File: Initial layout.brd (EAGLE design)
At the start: 152.4 x 127 mm, 50 parts, among them U2 TPS54540DDARQ1

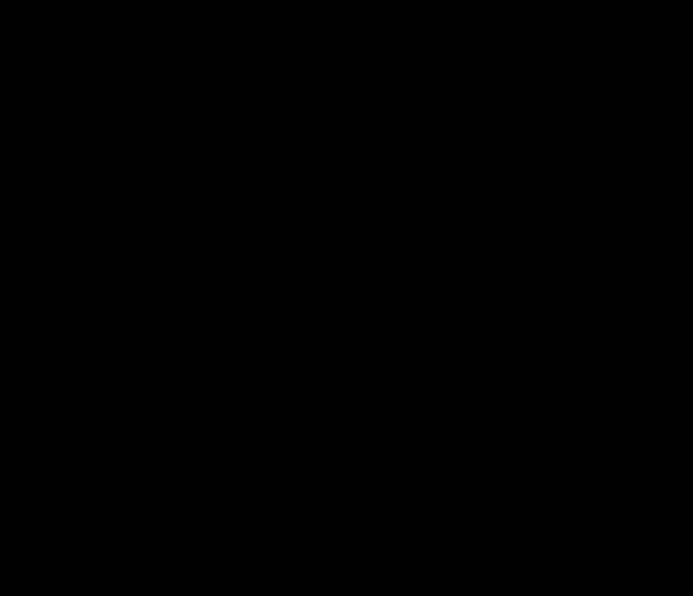
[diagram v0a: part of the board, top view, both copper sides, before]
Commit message: Added 4 pin clickmate for rj45
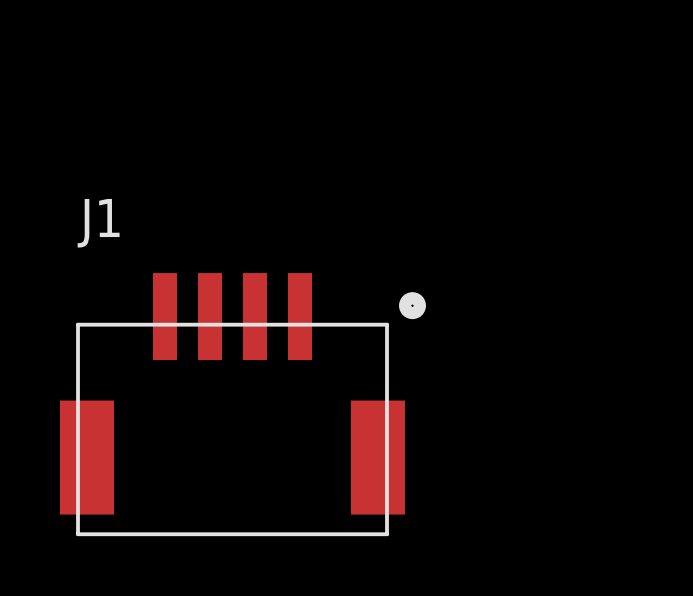
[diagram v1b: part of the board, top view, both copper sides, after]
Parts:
- added J1: 502585-0470, FormE:MOLEX-CLIKMATE-4-R/A
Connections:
- new net N$34: J1.1, U$2.38/A19
- new net N$35: J1.2, U$2.39/A20
- net GND: now also J1.3, J1.4
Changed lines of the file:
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@@
 <?xml version="1.0" encoding="utf-8"?>
 <!DOCTYPE eagle SYSTEM "eagle.dtd">
-<eagle version="8.5.0">
+<eagle version="8.6.0">
 <drawing>
 <settings>
@@
 <layers>
 <layer number="1" name="Top" color="4" fill="1" visible="yes" active="yes"/>
+<layer number="2" name="GND" color="11" fill="1" visible="yes" active="yes"/>
+<layer number="3" name="Route3" color="4" fill="3" visible="no" active="no"/>
+<layer number="4" name="Route4" color="1" fill="4" visible="no" active="no"/>
+<layer number="5" name="Route5" color="4" fill="4" visible="no" active="no"/>
+<layer number="6" name="Route6" color="1" fill="8" visible="no" active="no"/>
+<layer number="7" name="Route7" color="4" fill="8" visible="no" active="no"/>
+<layer number="8" name="Route8" color="1" fill="2" visible="no" active="no"/>
+<layer number="9" name="Route9" color="4" fill="2" visible="no" active="no"/>
+<layer number="10" name="Route10" color="1" fill="7" visible="no" active="no"/>
+<layer number="11" name="Route11" color="4" fill="7" visible="no" active="no"/>
+<layer number="12" name="Route12" color="1" fill="5" visible="no" active="no"/>
+<layer number="13" name="Route13" color="4" fill="5" visible="no" active="no"/>
+<layer number="14" name="Route14" color="1" fill="6" visible="no" active="no"/>
+<layer number="15" name="SUPPLY" color="13" fill="1" visible="yes" active="yes"/>
 <layer number="16" name="Bottom" color="1" fill="1" visible="yes" active="yes"/>
 <layer number="17" name="Pads" color="2" fill="1" visible="yes" active="yes"/>
@@
 </element>
 <element name="U3" library="FormE" package="SOIC8-N_MC" value="" x="8.25" y="87.41"/>
+<element name="J1" library="FormE" package="MOLEX-CLIKMATE-4-R/A" value="502585-0470" x="-7" y="26"/>
 </elements>
 <signals>
@@
 <wire x1="5.65" y1="88.045" x2="2.825" y2="88.045" width="0.254" layer="1"/>
 <wire x1="2.825" y1="88.045" x2="2.62" y2="88.25" width="0.254" layer="1"/>
+<contactref element="J1" pad="3"/>
+<contactref element="J1" pad="4"/>
 <wire x1="218" y1="39.43" x2="214.04" y2="39.78" width="0" layer="19" extent="1-1"/>
 <wire x1="206.98" y1="39.41" x2="214.04" y2="39.78" width="0" layer="19" extent="1-1"/>
@@
 <wire x1="5.65" y1="88.045" x2="10.85" y2="89.315" width="0" layer="19" extent="1-1"/>
 <wire x1="14.38" y1="81.83" x2="10.85" y2="89.315" width="0" layer="19" extent="1-1"/>
+<wire x1="-7.75" y1="29.7" x2="14.38" y2="81.83" width="0" layer="19" extent="1-1"/>
+<wire x1="-9.25" y1="29.7" x2="-7.75" y2="29.7" width="0" layer="19" extent="1-1"/>
 </signal>
 <signal name="+15V">
@@
 <wire x1="220.22" y1="59.35" x2="80.46" y2="123.33" width="0" layer="19" extent="1-1"/>
 </signal>
+<signal name="N$34">
+<contactref element="J1" pad="1"/>
+<contactref element="U$2" pad="38/A19"/>
+<wire x1="-4.75" y1="29.7" x2="85.54" y2="123.33" width="0" layer="19" extent="1-1"/>
+</signal>
+<signal name="N$35">
+<contactref element="J1" pad="2"/>
+<contactref element="U$2" pad="39/A20"/>
+<wire x1="-6.25" y1="29.7" x2="88.08" y2="123.33" width="0" layer="19" extent="1-1"/>
+</signal>
 </signals>

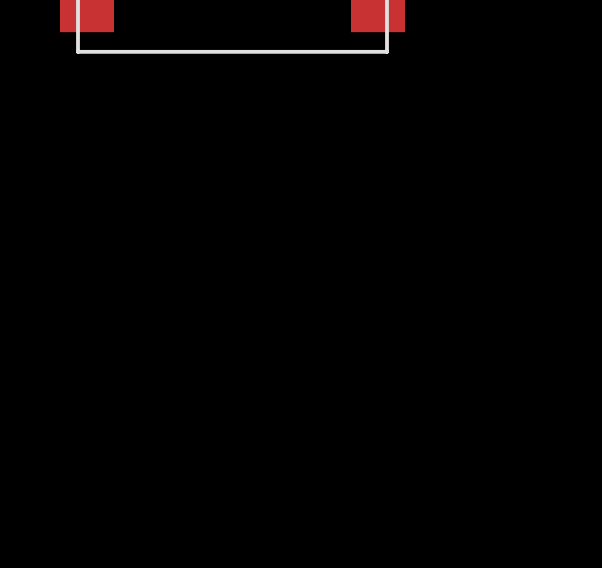
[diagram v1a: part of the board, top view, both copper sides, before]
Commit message: Added resistors for LEDs
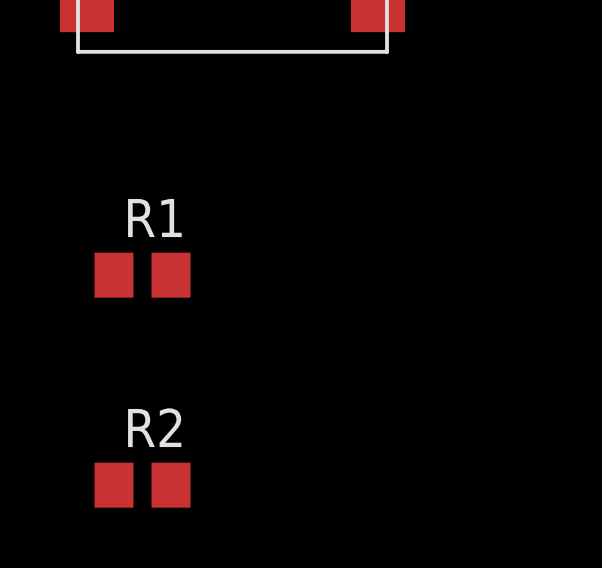
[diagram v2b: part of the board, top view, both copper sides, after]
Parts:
- added R1, R2: 100, rcl:R0805
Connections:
- new net N$41: R1.1, U$2.39/A20
- new net N$42: R2.1, U$2.38/A19
- net N$34: now also R2.2; no longer U$2.38/A19
- net N$35: now also R1.2; no longer U$2.39/A20
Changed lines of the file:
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@@
 <element name="U3" library="FormE" package="SOIC8-N_MC" value="" x="8.25" y="87.41"/>
 <element name="J1" library="FormE" package="MOLEX-CLIKMATE-4-R/A" value="502585-0470" x="-7" y="26"/>
+<element name="R1" library="rcl" package="R0805" value="100" x="-10" y="15"/>
+<element name="R2" library="rcl" package="R0805" value="100" x="-10" y="8"/>
 </elements>
 <signals>
@@
 <signal name="N$34">
 <contactref element="J1" pad="1"/>
-<contactref element="U$2" pad="38/A19"/>
-<wire x1="-4.75" y1="29.7" x2="85.54" y2="123.33" width="0" layer="19" extent="1-1"/>
+<contactref element="R2" pad="2"/>
+<wire x1="-9.05" y1="8" x2="-4.75" y2="29.7" width="0" layer="19" extent="1-1"/>
 </signal>
 <signal name="N$35">
 <contactref element="J1" pad="2"/>
+<contactref element="R1" pad="2"/>
+<wire x1="-9.05" y1="15" x2="-6.25" y2="29.7" width="0" layer="19" extent="1-1"/>
+</signal>
+<signal name="N$41">
 <contactref element="U$2" pad="39/A20"/>
-<wire x1="-6.25" y1="29.7" x2="88.08" y2="123.33" width="0" layer="19" extent="1-1"/>
+<contactref element="R1" pad="1"/>
+<wire x1="-10.95" y1="15" x2="88.08" y2="123.33" width="0" layer="19" extent="1-1"/>
+</signal>
+<signal name="N$42">
+<contactref element="U$2" pad="38/A19"/>
+<contactref element="R2" pad="1"/>
+<wire x1="-10.95" y1="8" x2="85.54" y2="123.33" width="0" layer="19" extent="1-1"/>
 </signal>
 </signals>

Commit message: Created Right Ear Board and made adjustments to Dash
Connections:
- removed net LBL: U$1.P$5, U$2.31/A12
- removed net RTDL: U$1.P$4, U$2.30
- new net NEO_PIXEL_PWM: U$1.P$4, U$2.21/A7
- new net SPARE_5: U$1.P$6
- net GND: now also U$1.P$5; no longer U$1.P$6
- net SERVO_PWM: now also U$2.22/A8; no longer U$2.29
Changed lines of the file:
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@@
 <contactref element="U$1" pad="P$19"/>
 <contactref element="U$1" pad="P$16"/>
-<contactref element="U$1" pad="P$6"/>
 <wire x1="5.65" y1="88.045" x2="2.825" y2="88.045" width="0.254" layer="1"/>
 <wire x1="2.825" y1="88.045" x2="2.62" y2="88.25" width="0.254" layer="1"/>
 <contactref element="J1" pad="3"/>
 <contactref element="J1" pad="4"/>
+<contactref element="U$1" pad="P$5"/>
 <wire x1="218" y1="39.43" x2="214.04" y2="39.78" width="0" layer="19" extent="1-1"/>
 <wire x1="206.98" y1="39.41" x2="214.04" y2="39.78" width="0" layer="19" extent="1-1"/>
@@
 <wire x1="236.05" y1="25.775" x2="227.34" y2="31.11" width="0" layer="19" extent="1-1"/>
 <wire x1="239.05" y1="26.41" x2="236.05" y2="25.775" width="0" layer="19" extent="1-1"/>
-<wire x1="224.22" y1="59.35" x2="218" y2="39.43" width="0" layer="19" extent="1-1"/>
-<wire x1="232.22" y1="67.35" x2="224.22" y2="59.35" width="0" layer="19" extent="1-1"/>
+<wire x1="228.22" y1="59.35" x2="218" y2="39.43" width="0" layer="19" extent="1-1"/>
+<wire x1="232.22" y1="67.35" x2="228.22" y2="59.35" width="0" layer="19" extent="1-1"/>
 <wire x1="244.22" y1="67.35" x2="232.22" y2="67.35" width="0" layer="19" extent="1-1"/>
 <wire x1="134.43" y1="36.84" x2="204.665" y2="31.22" width="0" layer="19" extent="1-1"/>
@@
 </signal>
 <signal name="SERVO_PWM">
-<contactref element="U$2" pad="29"/>
 <contactref element="U$1" pad="P$3"/>
-<wire x1="236.22" y1="59.35" x2="80.46" y2="108.09" width="0" layer="19" extent="1-1"/>
-</signal>
-<signal name="RTDL">
-<contactref element="U$1" pad="P$4"/>
-<contactref element="U$2" pad="30"/>
-<wire x1="232.22" y1="59.35" x2="77.92" y2="108.09" width="0" layer="19" extent="1-1"/>
-</signal>
-<signal name="LBL">
-<contactref element="U$1" pad="P$5"/>
-<contactref element="U$2" pad="31/A12"/>
-<wire x1="228.22" y1="59.35" x2="75.38" y2="108.09" width="0" layer="19" extent="1-1"/>
+<contactref element="U$2" pad="22/A8"/>
+<wire x1="236.22" y1="59.35" x2="121.1" y2="123.33" width="0" layer="19" extent="1-1"/>
 </signal>
 <signal name="N$27">
@@
 <wire x1="-10.95" y1="8" x2="85.54" y2="123.33" width="0" layer="19" extent="1-1"/>
 </signal>
+<signal name="NEO_PIXEL_PWM">
+<contactref element="U$1" pad="P$4"/>
+<contactref element="U$2" pad="21/A7"/>
+<wire x1="232.22" y1="59.35" x2="118.56" y2="123.33" width="0" layer="19" extent="1-1"/>
+</signal>
+<signal name="SPARE_5">
+<contactref element="U$1" pad="P$6"/>
+</signal>
 </signals>

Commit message: Defined Pins, Updated names on schematic
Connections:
- net N$13 renamed DOWN
- net N$15 renamed LEFT
- net N$17 renamed RIGHT
- net N$18 renamed DRS_FLAP
- net N$19 renamed UP
- net N$26 renamed CAN_RX
- net N$27 renamed DI1
- net N$28 renamed CAN_TX
- net N$3 renamed PADDLE
- net N$41 renamed RJ45_L1
- net N$42 renamed RJ45_L2
- removed net D2: JP2.6
- removed net N$16: U$2.3V3
- removed net NEO_PIXEL_PWM: U$1.P$4, U$2.21/A7
- new net DI2: JP2.6, U$1.P$4, U$2.21/A7
- net +3V3: now also U$2.3V3
- net SPARE_5: now also U$2.37/A18
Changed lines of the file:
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@@
 <contactref element="JP2" pad="5"/>
 </signal>
-<signal name="D2">
+<signal name="DI2">
 <contactref element="JP2" pad="6"/>
+<contactref element="U$1" pad="P$4"/>
+<contactref element="U$2" pad="21/A7"/>
+<wire x1="134.43" y1="72.4" x2="118.56" y2="123.33" width="0" layer="19" extent="1-1"/>
+<wire x1="232.22" y1="59.35" x2="134.43" y2="72.4" width="0" layer="19" extent="1-1"/>
 </signal>
 <signal name="D1">
@@
 <wire x1="10.85" y1="85.505" x2="12.625" y2="83.73" width="0.254" layer="1"/>
 <wire x1="12.625" y1="83.73" x2="14.38" y2="83.73" width="0.254" layer="1"/>
-</signal>
-<signal name="N$13">
+<contactref element="U$2" pad="3V3"/>
+<wire x1="14.38" y1="83.73" x2="95.7" y2="108.09" width="0" layer="19" extent="1-1"/>
+</signal>
+<signal name="DOWN">
 <contactref element="U$2" pad="25"/>
 </signal>
-<signal name="N$15">
+<signal name="LEFT">
 <contactref element="U$2" pad="26"/>
 </signal>
-<signal name="N$17">
+<signal name="RIGHT">
 <contactref element="U$2" pad="27"/>
 </signal>
-<signal name="N$18">
+<signal name="DRS_FLAP">
 <contactref element="U$2" pad="28"/>
 </signal>
@@
 <wire x1="242.22" y1="63.35" x2="14.38" y2="86.67" width="0" layer="19" extent="1-1"/>
 </signal>
-<signal name="N$3">
+<signal name="PADDLE">
 <contactref element="H1" pad="7"/>
 <contactref element="U$2" pad="32/A13"/>
 <wire x1="72.84" y1="108.09" x2="102.09" y2="101.474" width="0" layer="19" extent="1-1"/>
 </signal>
-<signal name="N$16">
-<contactref element="U$2" pad="3V3"/>
-</signal>
-<signal name="N$19">
+<signal name="UP">
 <contactref element="U$2" pad="24"/>
 </signal>
@@
 <wire x1="238.22" y1="63.35" x2="14.38" y2="88.57" width="0" layer="19" extent="1-1"/>
 </signal>
-<signal name="N$28">
+<signal name="CAN_TX">
 <contactref element="U3" pad="1"/>
 <contactref element="U$2" pad="3/CANTX"/>
 <wire x1="5.65" y1="89.315" x2="121.1" y2="108.09" width="0" layer="19" extent="1-1"/>
 </signal>
-<signal name="N$26">
+<signal name="CAN_RX">
 <contactref element="U3" pad="4"/>
 <contactref element="U$2" pad="4/CANRX"/>
@@
 <wire x1="236.22" y1="59.35" x2="121.1" y2="123.33" width="0" layer="19" extent="1-1"/>
 </signal>
-<signal name="N$27">
+<signal name="DI1">
 <contactref element="U$2" pad="2"/>
 <contactref element="LED1" pad="4-DIN"/>
@@
 <wire x1="-9.05" y1="15" x2="-6.25" y2="29.7" width="0" layer="19" extent="1-1"/>
 </signal>
-<signal name="N$41">
+<signal name="RJ45_L1">
 <contactref element="U$2" pad="39/A20"/>
 <contactref element="R1" pad="1"/>
 <wire x1="-10.95" y1="15" x2="88.08" y2="123.33" width="0" layer="19" extent="1-1"/>
 </signal>
-<signal name="N$42">
+<signal name="RJ45_L2">
 <contactref element="U$2" pad="38/A19"/>
 <contactref element="R2" pad="1"/>
 <wire x1="-10.95" y1="8" x2="85.54" y2="123.33" width="0" layer="19" extent="1-1"/>
 </signal>
-<signal name="NEO_PIXEL_PWM">
-<contactref element="U$1" pad="P$4"/>
-<contactref element="U$2" pad="21/A7"/>
-<wire x1="232.22" y1="59.35" x2="118.56" y2="123.33" width="0" layer="19" extent="1-1"/>
-</signal>
 <signal name="SPARE_5">
 <contactref element="U$1" pad="P$6"/>
+<contactref element="U$2" pad="37/A18"/>
+<wire x1="224.22" y1="59.35" x2="83" y2="123.33" width="0" layer="19" extent="1-1"/>
 </signal>
 </signals>

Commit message: Updated board layout
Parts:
- moved H1 277.9 mm to (-78.0, -111.0)
- moved C1 254.1 mm to (-102.5, -77.2)
- moved C10 254.1 mm to (59.5, -176.8)
- moved C11 254.1 mm to (-19.5, -68.3)
- moved C12 254.1 mm to (62.6, -176.8)
- moved C13 254.1 mm to (-9.49, -71.2)
- moved C14 254.1 mm to (3.51, -76.2)
- moved C15 254.1 mm to (11.5, -80.1)
- moved C16 254.1 mm to (-111.5, -84.0)
- moved C18 254.1 mm to (65.6, -178.8)
- moved C19 254.1 mm to (-143.4, -120.7)
- moved C2 254.1 mm to (-91.5, -70.4)
- moved C20 254.1 mm to (-131.6, -125.2)
- moved C24 254.1 mm to (59.7, -181.6)
- moved C25 254.1 mm to (64.3, -182.2)
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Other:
- board size 152.4 x 127 mm -> 159 x 109.2 mm

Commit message: Updated schematic and board layout
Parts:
- added H2, H3: 5025840870, FormE:MOLEX-CLIKMATE-8-VERTICAL-HEADER
- JP1: device adafruit:1X20 -> pinhead:1X08
- JP2: device adafruit:1X20 -> pinhead:1X01
- moved U$1 230.6 mm to (0.00, 70.0), turned to 180 degrees
- moved JP2 177.6 mm to (-151.1, -256.9), turned to 0 degrees
- moved JP1 116.4 mm to (-142.2, -241.7), turned to 0 degrees
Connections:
- removed net BACKLITE: JP2.13
- removed net C/D: JP2.17
- removed net CARD_CS: JP1.2
- removed net CARD_DETECT: JP1.1
- removed net D0: JP2.8
- removed net D1: JP2.7
- removed net D3: JP2.5
- removed net D4: JP2.4
- removed net D5: JP2.3
- removed net D6: JP2.2
- removed net D7: JP2.1
- removed net IM0: JP1.3
- removed net IM1: JP1.4
- removed net IM2: JP1.5
- removed net LITE: JP1.11
- removed net RD: JP2.15
- removed net RST: JP1.12, JP2.14
- removed net WR: JP2.16
- removed net X+: JP1.9, JP2.12
- removed net X-: JP1.7, JP2.10
- removed net Y+: JP1.10, JP2.11
- removed net Y-: JP1.8, JP2.9
- new net N$13: H3.2, JP1.2
- new net N$15: H3.3, JP1.3
- new net N$16: H3.4, JP1.4
- new net N$17: H3.5, JP1.5
- new net N$18: H3.6, JP1.6
- new net N$19: H3.7, JP1.7
- new net N$26: H3.8, JP1.8
- new net N$27: H2.6, JP2.1
- new net N$3: H3.1, JP1.1
- net +5V: now also H2.7; no longer JP1.19
- net CLK: now also H2.5; no longer JP1.17
- net CS: now also H2.2; no longer JP1.14, JP2.18
- net D/C: now also H2.1; no longer JP1.13
- net DI2: no longer JP2.6
- net GND: now also H2.8; no longer JP1.20, JP1.6, JP2.20
- net MISO: now also H2.4; no longer JP1.16
- net MOSI: now also H2.3; no longer JP1.15
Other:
- board size 159 x 109.2 mm -> 159 x 110.2 mm

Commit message: Finish board layout for main dash
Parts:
- moved JP2 331.9 mm to (14.4, 30.7)
- moved JP1 296.2 mm to (-41.9, 37.0), turned to 90 degrees
- moved R2 295.7 mm to (-47.8, 75.2), flipped to the bottom, turned to 180 degrees
- moved H3 291.5 mm to (-16.1, 31.5), flipped to the bottom, turned to 180 degrees
- moved R1 291.2 mm to (-47.8, 77.3), flipped to the bottom, turned to 180 degrees
- moved H2 287.2 mm to (2.41, 31.5), flipped to the bottom, turned to 180 degrees
- moved J1 283.1 mm to (-39.9, 77.6), flipped to the bottom, turned to 270 degrees
- moved R29 263.5 mm to (36.9, 77.8), flipped to the bottom, turned to 180 degrees
- moved U2 261.9 mm to (36.1, 74.1), flipped to the bottom
- moved R28 261.9 mm to (42.3, 77.4), flipped to the bottom, turned to 180 degrees
- moved C26 261.8 mm to (47.6, 76.7), flipped to the bottom, turned to 270 degrees
- moved C25 259.6 mm to (44.8, 76.7), flipped to the bottom, turned to 270 degrees
- moved C24 258.6 mm to (52.0, 76.8), flipped to the bottom, turned to 180 degrees
- moved C12 251.5 mm to (46.6, 74.2), flipped to the bottom
- moved C18 251.2 mm to (36.2, 70.6), flipped to the bottom
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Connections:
- net CANH1 renamed CAN_P
- net CANL1 renamed CAN_N
- removed net N$11: H1.1
- removed net N$20: H1.2
- removed net N$21: H1.3
- removed net N$22: H1.4
- removed net N$23: H1.5
- removed net N$24: H1.6
- net +3V3: now also H1.1
- net DOWN: now also H1.3
- net DRS_FLAP: now also H1.6
- net LEFT: now also H1.4
- net RIGHT: now also H1.5
- net UP: now also H1.2
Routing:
- net +5V: track 32.1 -> 368.8 mm, vias 12 -> 16
- net DI1: track 0.00 -> 93.9 mm, vias 0 -> 2
- net +15V: track 0.00 -> 88.3 mm, vias 0 -> 1
- net CAN_RX: track 0.00 -> 85.3 mm, vias 0 -> 3
- net CAN_TX: track 0.00 -> 80.1 mm, vias 0 -> 3
- net +3V3: track 4.27 -> 78.8 mm, vias 0 -> 1
- net RJ45_L1: track 0.00 -> 68.1 mm, vias 0 -> 3
- net SPARE_3: track 0.00 -> 63.6 mm, vias 0 -> 2
- net RJ45_L2: track 0.00 -> 61.4 mm, vias 0 -> 3
- net UP: track 0.00 -> 56.3 mm, vias 0 -> 3
- net SPARE_4: track 0.00 -> 55.8 mm, vias 0 -> 2
- net DOWN: track 0.00 -> 54.4 mm, vias 0 -> 3
- net RIGHT: track 0.00 -> 53.2 mm, vias 0 -> 2
- net LEFT: track 0.00 -> 52.2 mm, vias 0 -> 3
- net DRS_FLAP: track 0.00 -> 50.4 mm, vias 0 -> 3
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- added copper zone on layer 1, net GND
- added copper zone on layer 16, net GND
- added copper zone on layer 16, net SW_5V
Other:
- board size 159 x 110.2 mm -> 159 x 86.7 mm
